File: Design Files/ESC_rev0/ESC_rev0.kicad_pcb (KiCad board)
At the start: 4 copper layers, 100 x 75 mm, 175 parts, among them J1 Conn_01x08, J2 Conn_01x06, J3 Conn_01x03, J4 WP-BUTR, J5 WP-BUTR, J6 WP-BUTR, J7 Conn_01x04, J8 Conn_01x06, J9 USB_C_Receptacle_USB2.0_16P, Q1 HSBA15810C, Q2 HSBA15810C, Q3 HSBA15810C, Q4 HSBA15810C, Q5 HSBA15810C, Q6 HSBA15810C, SW1 Push Button, U1 XT60PW-M, U2 XH-2PWBPZ, U3 AMS1117-3.3, U4 STM32F405RGTx, U5 DRV8302DCA, U6 ESDCAN24-2BLY, U7 SN65HVD230, Y1 Crystal

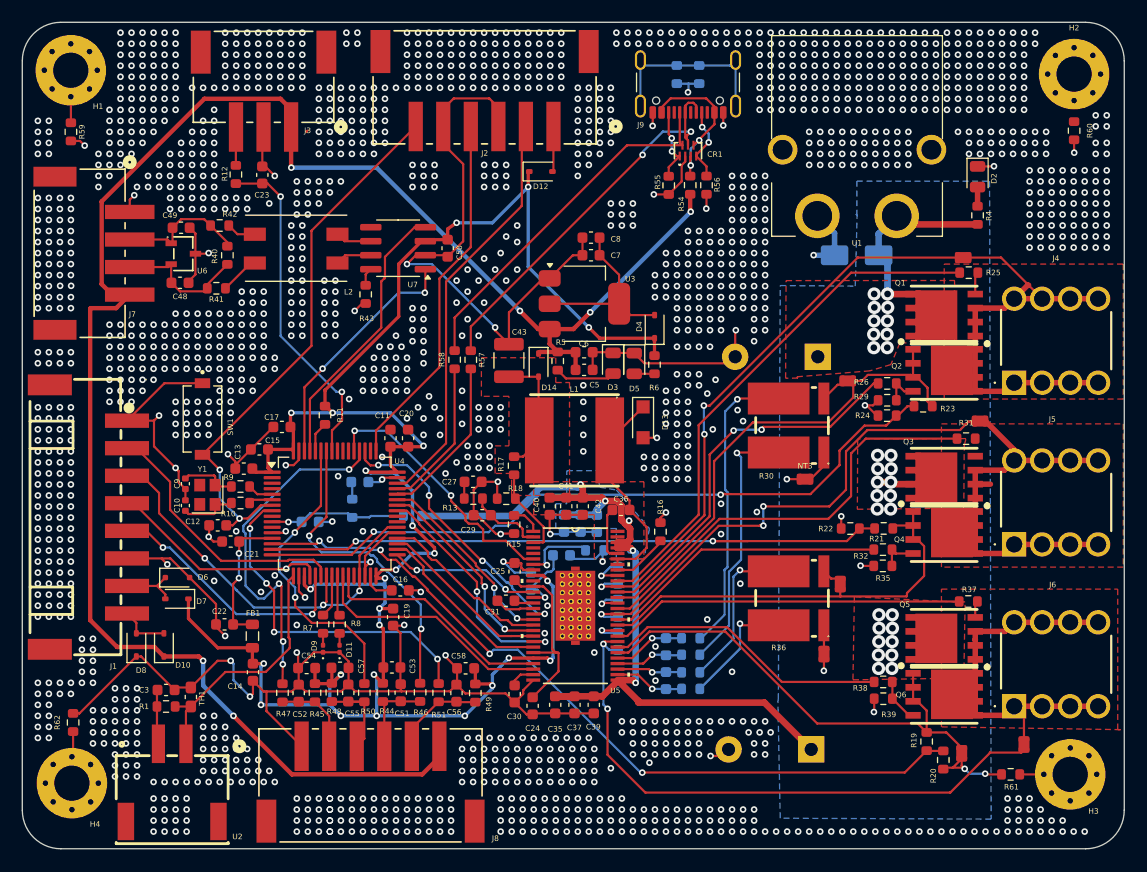
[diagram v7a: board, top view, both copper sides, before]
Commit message: update 21
DRC checked, all problems solved. Created Custom Rules to following JLCPCB most important capabilities. Relevant modifications on tracks, components positions and to copper pours were made. Board images were updated in the schematics.
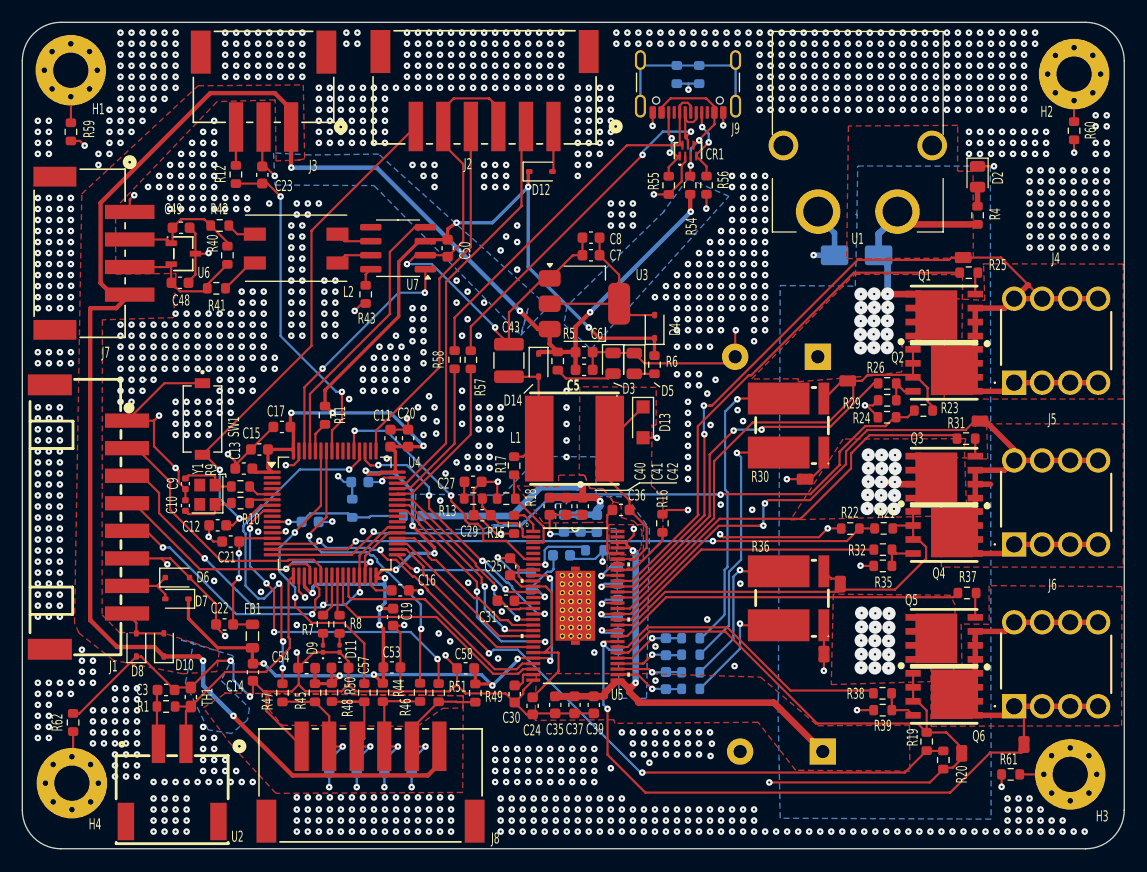
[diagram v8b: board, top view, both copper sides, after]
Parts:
- C51, C52, C55, C56: moved to B.Cu
- J9: footprint Connector_USB:USB_C_Receptacle_GCT_USB4105-xx-A_16P_TopMnt_Horizontal -> Connector_USB:USB_C_Receptacle_GCT_USB4105-xx-A_16P_TopMnt_Horizontal_mod
- moved C56 7.60 mm to (114.9, 122.4), turned to -90 degrees
- moved C52 6.99 mm to (107.4, 122.4), turned to -90 degrees
- moved C51 6.63 mm to (112.5, 122.4), turned to -90 degrees
- moved C55 6.48 mm to (109.9, 122.4), turned to -90 degrees
- moved C1 1.07 mm to (152.2, 121.2)
- moved R39 1.04 mm to (157.7, 117.5)
- moved R38 1.03 mm to (157.7, 116.0)
- moved R16 0.78 mm to (137.7, 100.5)
- moved R37 0.78 mm to (165.3, 106.8)
- moved C25 0.59 mm to (123.9, 104.5)
- moved R23 0.39 mm to (161.4, 90.3)
- moved U1 0.39 mm to (155.4, 72.2)
- moved L1 0.16 mm to (129.7, 92.8)
- moved R24 0.15 mm to (158.1, 90.9)
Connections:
- U5 pad V: (no net) -> GND
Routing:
- net GND: track 298.1 -> 332.1 mm, vias 1790 -> 1566
- net +3V3: track 197.1 -> 185.6 mm, vias 25 -> 21
- net +5V: track 165.7 -> 170.8 mm
- net +VDC: track 101.1 -> 96.6 mm, vias 35 -> 50
- net Net-(H2-Pad1): track 0.00 -> 4.31 mm
- net SENS2: track 58.6 -> 55.5 mm
- net /Filters/TEMP_IN: track 8.39 -> 11.2 mm, vias 0 -> 1
- net /Filters/HALL_2_IN: track 8.74 -> 11.6 mm, vias 0 -> 1
- net /Filters/HALL_1_IN: track 7.50 -> 10.3 mm, vias 0 -> 1
- net /Filters/HALL_3_IN: track 7.52 -> 10.3 mm, vias 0 -> 1
- net /USB/USB-C_P: track 33.2 -> 35.7 mm
- net /MOSFETs/GH2_RG: track 0.00 -> 1.60 mm
- net GH2: track 39.5 -> 38.2 mm
- net SH2: track 46.2 -> 45.0 mm
- net SL2: track 38.9 -> 37.9 mm
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- added copper zone on B.Cu, net +5V
- added copper zone on F.Cu, net /MOSFET DRIVER/PH
